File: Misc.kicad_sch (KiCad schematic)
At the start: 0 parts

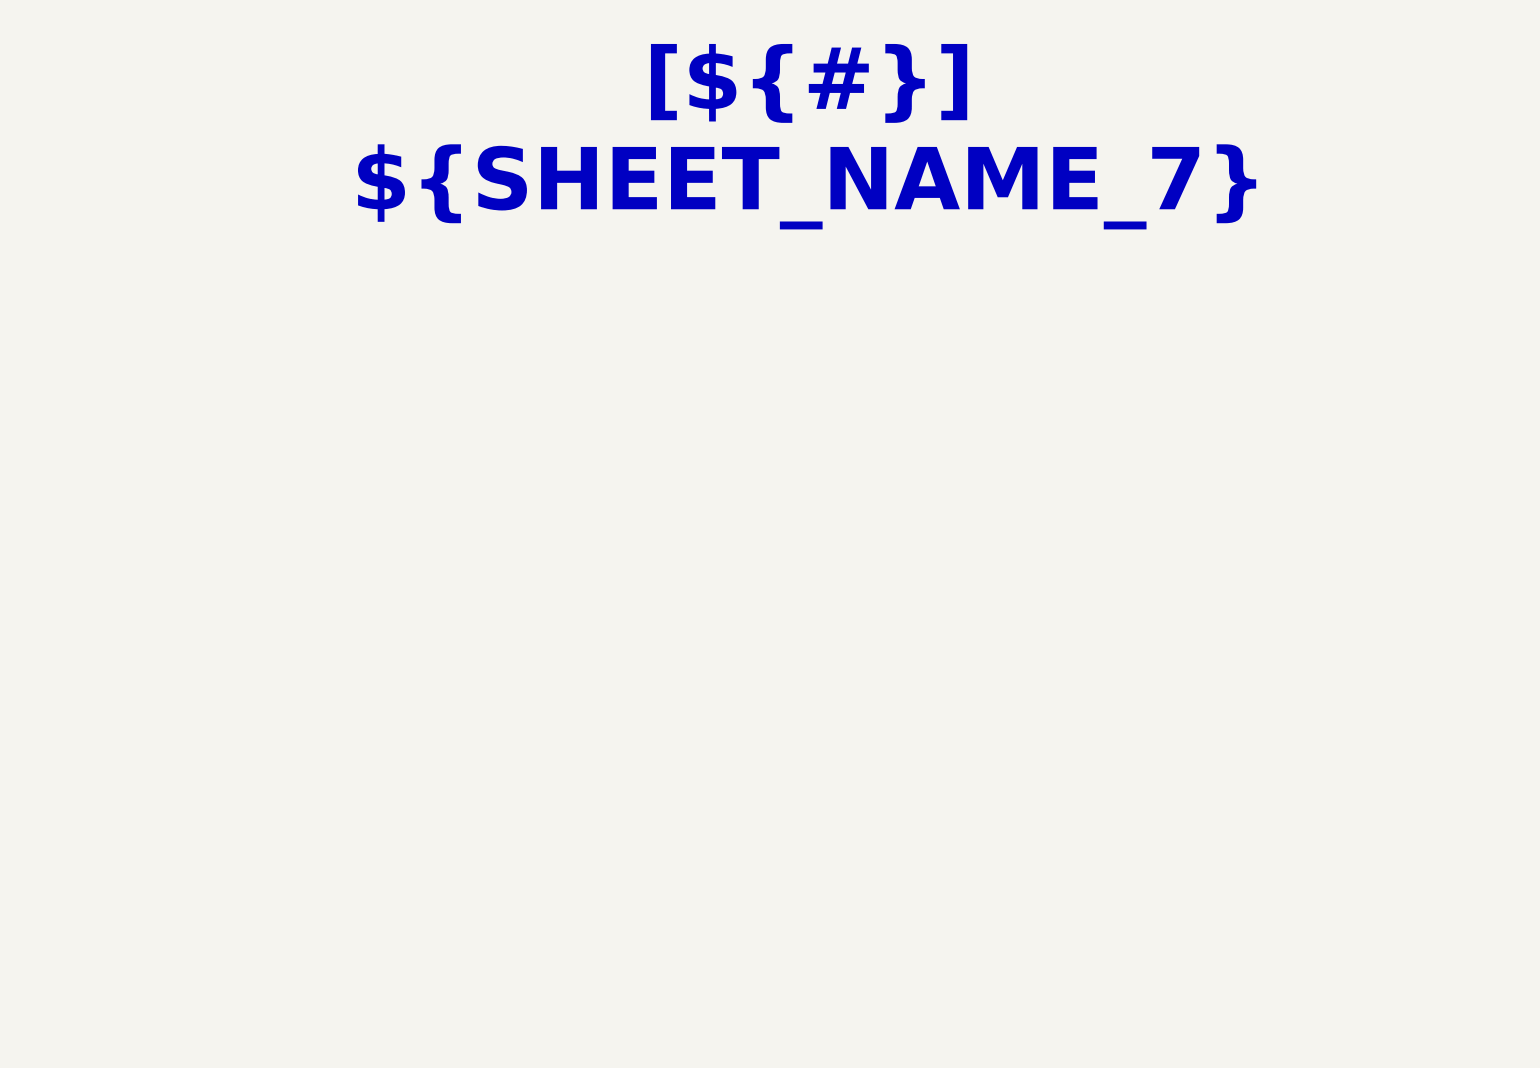
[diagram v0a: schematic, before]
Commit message: Pasted schematics from previous design
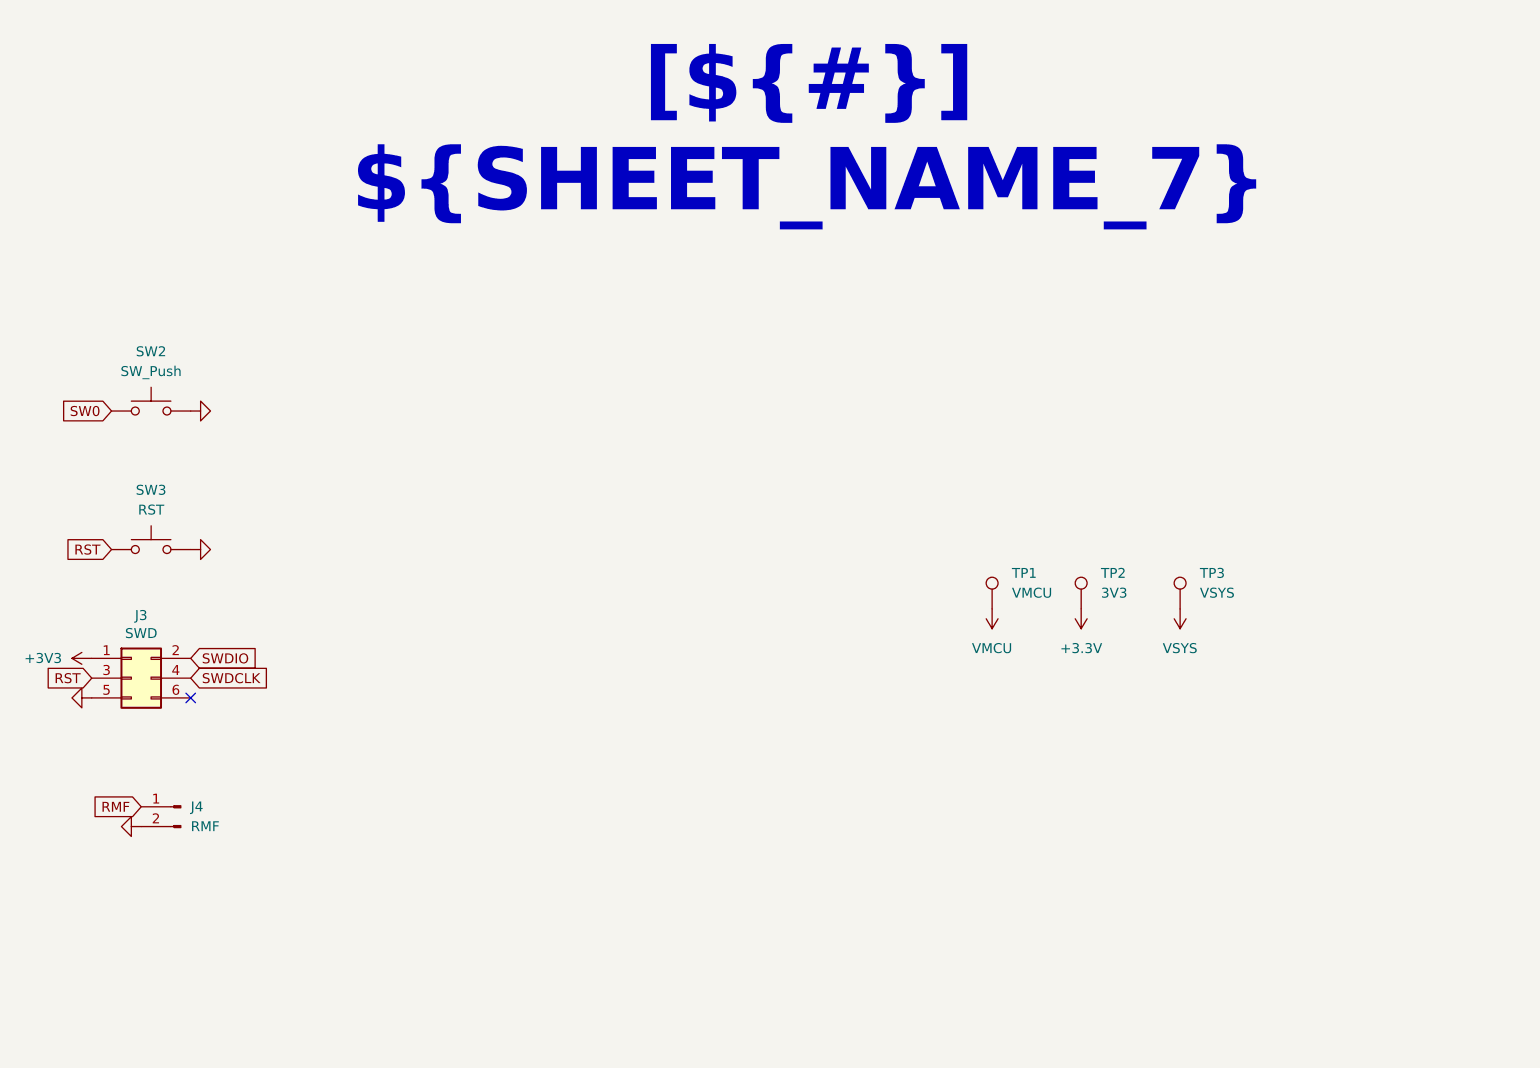
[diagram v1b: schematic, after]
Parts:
- added J3: SWD, Connector_PinHeader_2.54mm:PinHeader_2x03_P2.54mm_Vertical, symbol Connector_Generic:Conn_02x03_Odd_Even
- added J4: RMF, Connector_PinHeader_2.54mm:PinHeader_1x02_P2.54mm_Vertical, symbol Connector:Conn_01x02_Pin
- added SW2: SW_Push, Button_Switch_SMD:SW_Push_1P1T_NO_CK_KMR2, symbol Switch:SW_Push
- added SW3: RST, Button_Switch_SMD:SW_Push_1P1T_NO_CK_KMR2, symbol Switch:SW_Push
- added TP1: VMCU, TestPoint:TestPoint_Pad_D1.0mm, symbol Connector:TestPoint
- added TP2: 3V3, TestPoint:TestPoint_Pad_D1.0mm, symbol Connector:TestPoint
- added TP3: VSYS, TestPoint:TestPoint_Pad_D1.0mm, symbol Connector:TestPoint
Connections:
- new net +3.3V: TP2.1
- new net +3V3: J3.1 (Pin_1)
- new net GND: J3.5 (Pin_5), J4.2 (Pin_2), SW2.2, SW3.2
- new net RMF: J4.1 (Pin_1)
- new net RST: J3.3 (Pin_3), SW3.1
- new net SW0: SW2.1
- new net SWDCLK: J3.4 (Pin_4)
- new net SWDIO: J3.2 (Pin_2)
- new net VMCU: TP1.1
- new net VSYS: TP3.1
- no-connect marks 0 -> 1

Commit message: Finished preliminary project schematics and architecture
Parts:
- renumbered J3 to J2, J4 to J3
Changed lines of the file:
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@@
 		(at 66.04 96.52)
+	)
+	(bus_entry
+		(at 101.6 96.52)
+		(size 2.54 2.54)
+		(stroke
+			(width 0)
+			(type default)
+		)
+	)
+	(bus_entry
+		(at 101.6 104.14)
+		(size 2.54 2.54)
+		(stroke
+			(width 0)
+			(type default)
+		)
+	)
+	(bus_entry
+		(at 101.6 101.6)
+		(size 2.54 2.54)
+		(stroke
+			(width 0)
+			(type default)
+		)
+	)
+	(bus_entry
+		(at 101.6 99.06)
+		(size 2.54 2.54)
+		(stroke
+			(width 0)
+			(type default)
+		)
+	)
+	(wire
+		(pts
+			(xy 104.14 106.68) (xy 105.41 106.68)
+		)
+		(stroke
+			(width 0)
+			(type default)
+		)
+	)
+	(wire
+		(pts
+			(xy 104.14 101.6) (xy 105.41 101.6)
+		)
+		(stroke
+			(width 0)
+			(type default)
+		)
+	)
+	(wire
+		(pts
+			(xy 104.14 99.06) (xy 105.41 99.06)
+		)
+		(stroke
+			(width 0)
+			(type default)
+		)
+	)
+	(wire
+		(pts
+			(xy 104.14 104.14) (xy 105.41 104.14)
+		)
+		(stroke
+			(width 0)
+			(type default)
+		)
+	)
+	(bus
+		(pts
+			(xy 101.6 91.44) (xy 101.6 104.14)
+		)
+		(stroke
+			(width 0)
+			(type default)
+		)
+	)
+	(global_label "SWDIO"
+		(shape input)
+		(at 105.41 104.14 0)
+		(fields_autoplaced yes)
+		(effects
+			(font
+				(size 1.27 1.27)
+			)
+			(justify left)
+		)
+		(property "Intersheetrefs" "${INTERSHEET_REFS}"
+			(at 114.2614 104.14 0)
+			(hide yes)
+			(show_name no)
+			(do_not_autoplace no)
+			(effects
+				(font
+					(size 1.27 1.27)
+				)
+				(justify left)
+			)
+		)
+	)
+	(global_label "SWDCLK"
+		(shape input)
+		(at 105.41 106.68 0)
+		(fields_autoplaced yes)
+		(effects
+			(font
+				(size 1.27 1.27)
+			)
+			(justify left)
+		)
+		(property "Intersheetrefs" "${INTERSHEET_REFS}"
+			(at 115.8942 106.68 0)
+			(hide yes)
+			(show_name no)
+			(do_not_autoplace no)
+			(effects
+				(font
+					(size 1.27 1.27)
+				)
+				(justify left)
+			)
+		)
 	)
 	(global_label "RST"
@@
 		)
 	)
-	(global_label "RMF"
+	(global_label "SW0"
 		(shape input)
-		(at 59.69 110.49 180)
+		(at 105.41 99.06 0)
 		(fields_autoplaced yes)
 		(effects
@@
 				(size 1.27 1.27)
 			)
-			(justify right)
+			(justify left)
 		)
 		(property "Intersheetrefs" "${INTERSHEET_REFS}"
-			(at 52.8948 110.49 0)
-			(hide yes)
-			(show_name no)
-			(do_not_autoplace no)
-			(effects
-				(font
-					(size 1.27 1.27)
-				)
-				(justify right)
+			(at 112.2656 99.06 0)
+			(hide yes)
+			(show_name no)
+			(do_not_autoplace no)
+			(effects
+				(font
+					(size 1.27 1.27)
+				)
+				(justify left)
 			)
 		)
@@
 				(justify left)
 			)
+		)
+	)
+	(global_label "RST"
+		(shape input)
+		(at 105.41 101.6 0)
+		(fields_autoplaced yes)
+		(effects
+			(font
+				(size 1.27 1.27)
+			)
+			(justify left)
+		)
+		(property "Intersheetrefs" "${INTERSHEET_REFS}"
+			(at 111.8423 101.6 0)
+			(hide yes)
+			(show_name no)
+			(do_not_autoplace no)
+			(effects
+				(font
+					(size 1.27 1.27)
+				)
+				(justify left)
+			)
+		)
+	)
+	(hierarchical_label "{Prog_BUS}"
+		(shape input)
+		(at 101.6 91.44 90)
+		(effects
+			(font
+				(size 1.27 1.27)
+			)
+			(justify left)
+		)
+	)
+	(hierarchical_label "RMF"
+		(shape input)
+		(at 59.69 110.49 180)
+		(effects
+			(font
+				(size 1.27 1.27)
+			)
+			(justify right)
 		)
 	)
@@
 		(instances
 			(project "CanSat_Devboard"
-				(path "/f9e05184-c88b-4a88-ae9c-ab2bdb32be7c/1d8b8fa6-9111-4415-b516-c06d0094a485"
+				(path "/f9e05184-c88b-4a88-ae9c-ab2bdb32be7c/5d00bd0a-3bbf-46b2-b8c5-f75441fb4350/018262e7-802c-4bdf-a206-c30cacd206c9"
 					(reference "#PWR045")
 					(unit 1)
@@
 		(instances
 			(project "CanSat_Devboard"
-				(path "/f9e05184-c88b-4a88-ae9c-ab2bdb32be7c/1d8b8fa6-9111-4415-b516-c06d0094a485"
+				(path "/f9e05184-c88b-4a88-ae9c-ab2bdb32be7c/5d00bd0a-3bbf-46b2-b8c5-f75441fb4350/018262e7-802c-4bdf-a206-c30cacd206c9"
 					(reference "#PWR043")
 					(unit 1)
@@
 		(dnp no)
 		(fields_autoplaced yes)
-		(property "Reference" "J4"
+		(property "Reference" "J3"
 			(at 66.04 110.4899 0)
 			(show_name no)
@@
 		(instances
 			(project "CanSat_Devboard"
-				(path "/f9e05184-c88b-4a88-ae9c-ab2bdb32be7c/1d8b8fa6-9111-4415-b516-c06d0094a485"
-					(reference "J4")
+				(path "/f9e05184-c88b-4a88-ae9c-ab2bdb32be7c/5d00bd0a-3bbf-46b2-b8c5-f75441fb4350/018262e7-802c-4bdf-a206-c30cacd206c9"
+					(reference "J3")
 					(unit 1)
 				)
@@
 		(instances
 			(project "CanSat_Devboard"
-				(path "/f9e05184-c88b-4a88-ae9c-ab2bdb32be7c/1d8b8fa6-9111-4415-b516-c06d0094a485"
+				(path "/f9e05184-c88b-4a88-ae9c-ab2bdb32be7c/5d00bd0a-3bbf-46b2-b8c5-f75441fb4350/018262e7-802c-4bdf-a206-c30cacd206c9"
 					(reference "SW2")
 					(unit 1)
@@
 		(instances
 			(project "CanSat_Devboard"
-				(path "/f9e05184-c88b-4a88-ae9c-ab2bdb32be7c/1d8b8fa6-9111-4415-b516-c06d0094a485"
+				(path "/f9e05184-c88b-4a88-ae9c-ab2bdb32be7c/5d00bd0a-3bbf-46b2-b8c5-f75441fb4350/018262e7-802c-4bdf-a206-c30cacd206c9"
 					(reference "#PWR047")
 					(unit 1)
@@
 		(instances
 			(project "CanSat_Devboard"
-				(path "/f9e05184-c88b-4a88-ae9c-ab2bdb32be7c/1d8b8fa6-9111-4415-b516-c06d0094a485"
+				(path "/f9e05184-c88b-4a88-ae9c-ab2bdb32be7c/5d00bd0a-3bbf-46b2-b8c5-f75441fb4350/018262e7-802c-4bdf-a206-c30cacd206c9"
 					(reference "#PWR030")
 					(unit 1)
@@
 		(instances
 			(project "CanSat_Devboard"
-				(path "/f9e05184-c88b-4a88-ae9c-ab2bdb32be7c/1d8b8fa6-9111-4415-b516-c06d0094a485"
+				(path "/f9e05184-c88b-4a88-ae9c-ab2bdb32be7c/5d00bd0a-3bbf-46b2-b8c5-f75441fb4350/018262e7-802c-4bdf-a206-c30cacd206c9"
 					(reference "TP2")
 					(unit 1)
@@
 		(instances
 			(project "CanSat_Devboard"
-				(path "/f9e05184-c88b-4a88-ae9c-ab2bdb32be7c/1d8b8fa6-9111-4415-b516-c06d0094a485"
+				(path "/f9e05184-c88b-4a88-ae9c-ab2bdb32be7c/5d00bd0a-3bbf-46b2-b8c5-f75441fb4350/018262e7-802c-4bdf-a206-c30cacd206c9"
 					(reference "#PWR046")
 					(unit 1)
@@
 		(in_pos_files yes)
 		(dnp no)
-		(property "Reference" "J3"
+		(property "Reference" "J2"
 			(at 59.69 85.9282 0)
 			(show_name no)
@@
 		(instances
 			(project "CanSat_Devboard"
-				(path "/f9e05184-c88b-4a88-ae9c-ab2bdb32be7c/1d8b8fa6-9111-4415-b516-c06d0094a485"
-					(reference "J3")
+				(path "/f9e05184-c88b-4a88-ae9c-ab2bdb32be7c/5d00bd0a-3bbf-46b2-b8c5-f75441fb4350/018262e7-802c-4bdf-a206-c30cacd206c9"
+					(reference "J2")
 					(unit 1)
 				)
@@
 		(instances
 			(project "CanSat_Devboard"
-				(path "/f9e05184-c88b-4a88-ae9c-ab2bdb32be7c/1d8b8fa6-9111-4415-b516-c06d0094a485"
+				(path "/f9e05184-c88b-4a88-ae9c-ab2bdb32be7c/5d00bd0a-3bbf-46b2-b8c5-f75441fb4350/018262e7-802c-4bdf-a206-c30cacd206c9"
 					(reference "TP1")
 					(unit 1)
@@
 		(instances
 			(project "CanSat_Devboard"
-				(path "/f9e05184-c88b-4a88-ae9c-ab2bdb32be7c/1d8b8fa6-9111-4415-b516-c06d0094a485"
+				(path "/f9e05184-c88b-4a88-ae9c-ab2bdb32be7c/5d00bd0a-3bbf-46b2-b8c5-f75441fb4350/018262e7-802c-4bdf-a206-c30cacd206c9"
 					(reference "#PWR042")
 					(unit 1)
@@
 		(instances
 			(project "CanSat_Devboard"
-				(path "/f9e05184-c88b-4a88-ae9c-ab2bdb32be7c/1d8b8fa6-9111-4415-b516-c06d0094a485"
+				(path "/f9e05184-c88b-4a88-ae9c-ab2bdb32be7c/5d00bd0a-3bbf-46b2-b8c5-f75441fb4350/018262e7-802c-4bdf-a206-c30cacd206c9"
 					(reference "TP3")
 					(unit 1)
@@
 		(instances
 			(project "CanSat_Devboard"
-				(path "/f9e05184-c88b-4a88-ae9c-ab2bdb32be7c/1d8b8fa6-9111-4415-b516-c06d0094a485"
+				(path "/f9e05184-c88b-4a88-ae9c-ab2bdb32be7c/5d00bd0a-3bbf-46b2-b8c5-f75441fb4350/018262e7-802c-4bdf-a206-c30cacd206c9"
 					(reference "#PWR044")
 					(unit 1)
@@
 		(instances
 			(project "CanSat_Devboard"
-				(path "/f9e05184-c88b-4a88-ae9c-ab2bdb32be7c/1d8b8fa6-9111-4415-b516-c06d0094a485"
+				(path "/f9e05184-c88b-4a88-ae9c-ab2bdb32be7c/5d00bd0a-3bbf-46b2-b8c5-f75441fb4350/018262e7-802c-4bdf-a206-c30cacd206c9"
 					(reference "SW3")
 					(unit 1)
@@
 		(instances
 			(project "CanSat_Devboard"
-				(path "/f9e05184-c88b-4a88-ae9c-ab2bdb32be7c/1d8b8fa6-9111-4415-b516-c06d0094a485"
+				(path "/f9e05184-c88b-4a88-ae9c-ab2bdb32be7c/5d00bd0a-3bbf-46b2-b8c5-f75441fb4350/018262e7-802c-4bdf-a206-c30cacd206c9"
 					(reference "#PWR034")
 					(unit 1)

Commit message: Edited ci.yaml
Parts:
- added BT2: 1S Lipo, Connector_JST:JST_XH_B2B-XH-A_1x02_P2.50mm_Vertical, symbol Device:Battery_Cell
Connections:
- net GND: now also BT2.2 (-)
- new net VBAT: BT2.1 (+)

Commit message: Cleaned up
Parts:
- renumbered BT2 to BT1, SW2 to SW1, SW3 to SW2
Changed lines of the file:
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@@
 		(in_pos_files yes)
 		(dnp no)
-		(property "Reference" "#PWR045"
+		(property "Reference" "#PWR010"
 			(at 72.39 59.69 0)
 			(hide yes)
@@
 			(project "CanSat_Devboard"
 				(path "/f9e05184-c88b-4a88-ae9c-ab2bdb32be7c/5d00bd0a-3bbf-46b2-b8c5-f75441fb4350/018262e7-802c-4bdf-a206-c30cacd206c9"
-					(reference "#PWR045")
+					(reference "#PWR010")
 					(unit 1)
 				)
@@
 		(in_pos_files yes)
 		(dnp no)
-		(property "Reference" "#PWR043"
+		(property "Reference" "#PWR016"
 			(at 46.99 96.52 0)
 			(hide yes)
@@
 			(project "CanSat_Devboard"
 				(path "/f9e05184-c88b-4a88-ae9c-ab2bdb32be7c/5d00bd0a-3bbf-46b2-b8c5-f75441fb4350/018262e7-802c-4bdf-a206-c30cacd206c9"
-					(reference "#PWR043")
+					(reference "#PWR016")
 					(unit 1)
 				)
@@
 		(dnp no)
 		(fields_autoplaced yes)
-		(property "Reference" "SW2"
+		(property "Reference" "SW1"
 			(at 60.96 52.07 0)
 			(show_name no)
@@
 			(project "CanSat_Devboard"
 				(path "/f9e05184-c88b-4a88-ae9c-ab2bdb32be7c/5d00bd0a-3bbf-46b2-b8c5-f75441fb4350/018262e7-802c-4bdf-a206-c30cacd206c9"
-					(reference "SW2")
+					(reference "SW1")
 					(unit 1)
 				)
@@
 		(dnp no)
 		(fields_autoplaced yes)
-		(property "Reference" "#PWR047"
+		(property "Reference" "#PWR014"
 			(at 193.04 81.28 0)
 			(hide yes)
@@
 			(project "CanSat_Devboard"
 				(path "/f9e05184-c88b-4a88-ae9c-ab2bdb32be7c/5d00bd0a-3bbf-46b2-b8c5-f75441fb4350/018262e7-802c-4bdf-a206-c30cacd206c9"
-					(reference "#PWR047")
+					(reference "#PWR014")
 					(unit 1)
 				)
@@
 		(dnp no)
 		(fields_autoplaced yes)
-		(property "Reference" "#PWR030"
+		(property "Reference" "#PWR012"
 			(at 168.91 81.28 0)
 			(hide yes)
@@
 			(project "CanSat_Devboard"
 				(path "/f9e05184-c88b-4a88-ae9c-ab2bdb32be7c/5d00bd0a-3bbf-46b2-b8c5-f75441fb4350/018262e7-802c-4bdf-a206-c30cacd206c9"
-					(reference "#PWR030")
+					(reference "#PWR012")
 					(unit 1)
 				)
@@
 		(dnp no)
 		(fields_autoplaced yes)
-		(property "Reference" "#PWR049"
+		(property "Reference" "#PWR019"
 			(at 58.42 139.7 0)
 			(hide yes)
@@
 			(project "CanSat_Devboard"
 				(path "/f9e05184-c88b-4a88-ae9c-ab2bdb32be7c/5d00bd0a-3bbf-46b2-b8c5-f75441fb4350/018262e7-802c-4bdf-a206-c30cacd206c9"
-					(reference "#PWR049")
+					(reference "#PWR019")
 					(unit 1)
 				)
@@
 		(dnp no)
 		(fields_autoplaced yes)
-		(property "Reference" "#PWR046"
+		(property "Reference" "#PWR011"
 			(at 72.39 77.47 0)
 			(hide yes)
@@
 			(project "CanSat_Devboard"
 				(path "/f9e05184-c88b-4a88-ae9c-ab2bdb32be7c/5d00bd0a-3bbf-46b2-b8c5-f75441fb4350/018262e7-802c-4bdf-a206-c30cacd206c9"
-					(reference "#PWR046")
+					(reference "#PWR011")
 					(unit 1)
 				)
@@
 		(dnp no)
 		(fields_autoplaced yes)
-		(property "Reference" "#PWR042"
+		(property "Reference" "#PWR015"
 			(at 57.15 91.44 0)
 			(hide yes)
@@
 			(project "CanSat_Devboard"
 				(path "/f9e05184-c88b-4a88-ae9c-ab2bdb32be7c/5d00bd0a-3bbf-46b2-b8c5-f75441fb4350/018262e7-802c-4bdf-a206-c30cacd206c9"
-					(reference "#PWR042")
+					(reference "#PWR015")
 					(unit 1)
 				)
@@
 		(dnp no)
 		(fields_autoplaced yes)
-		(property "Reference" "#PWR048"
+		(property "Reference" "#PWR018"
 			(at 48.26 139.7 0)
 			(hide yes)
@@
 			(project "CanSat_Devboard"
 				(path "/f9e05184-c88b-4a88-ae9c-ab2bdb32be7c/5d00bd0a-3bbf-46b2-b8c5-f75441fb4350/018262e7-802c-4bdf-a206-c30cacd206c9"
-					(reference "#PWR048")
+					(reference "#PWR018")
 					(unit 1)
 				)
@@
 		(dnp no)
 		(fields_autoplaced yes)
-		(property "Reference" "BT2"
+		(property "Reference" "BT1"
 			(at 58.9915 132.08 90)
 			(show_name no)
@@
 			(project "CanSat_Devboard"
 				(path "/f9e05184-c88b-4a88-ae9c-ab2bdb32be7c/5d00bd0a-3bbf-46b2-b8c5-f75441fb4350/018262e7-802c-4bdf-a206-c30cacd206c9"
-					(reference "BT2")
+					(reference "BT1")
 					(unit 1)
 				)
@@
 		(in_pos_files yes)
 		(dnp no)
-		(property "Reference" "#PWR044"
+		(property "Reference" "#PWR017"
 			(at 53.34 113.03 0)
 			(hide yes)
@@
 			(project "CanSat_Devboard"
 				(path "/f9e05184-c88b-4a88-ae9c-ab2bdb32be7c/5d00bd0a-3bbf-46b2-b8c5-f75441fb4350/018262e7-802c-4bdf-a206-c30cacd206c9"
-					(reference "#PWR044")
+					(reference "#PWR017")
 					(unit 1)
 				)
@@
 		(dnp no)
 		(fields_autoplaced yes)
-		(property "Reference" "SW3"
+		(property "Reference" "SW2"
 			(at 60.96 69.85 0)
 			(show_name no)
@@
 			(project "CanSat_Devboard"
 				(path "/f9e05184-c88b-4a88-ae9c-ab2bdb32be7c/5d00bd0a-3bbf-46b2-b8c5-f75441fb4350/018262e7-802c-4bdf-a206-c30cacd206c9"
-					(reference "SW3")
+					(reference "SW2")
 					(unit 1)
 				)
@@
 		(dnp no)
 		(fields_autoplaced yes)
-		(property "Reference" "#PWR034"
+		(property "Reference" "#PWR013"
 			(at 180.34 81.28 0)
 			(hide yes)
@@
 			(project "CanSat_Devboard"
 				(path "/f9e05184-c88b-4a88-ae9c-ab2bdb32be7c/5d00bd0a-3bbf-46b2-b8c5-f75441fb4350/018262e7-802c-4bdf-a206-c30cacd206c9"
-					(reference "#PWR034")
-					(unit 1)
-				)
+					(reference "#PWR013")
+					(unit 1)
+				)
